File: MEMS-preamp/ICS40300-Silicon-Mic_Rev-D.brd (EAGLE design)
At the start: 14 x 15.7 mm, 8 parts, among them U1 ICS-40300, U2 MIC5225-3.3

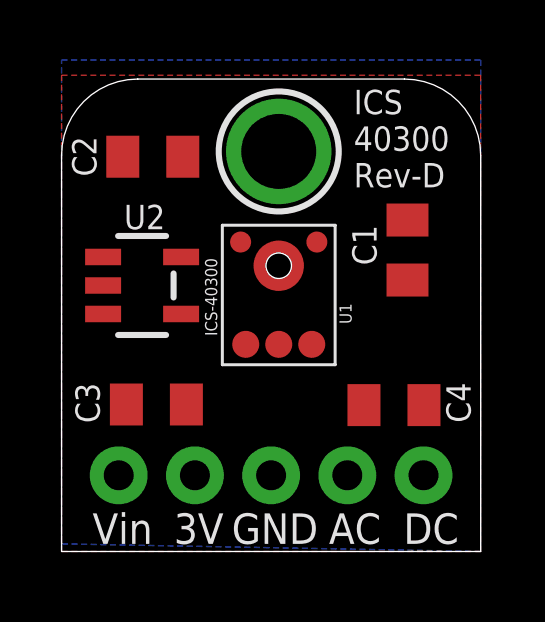
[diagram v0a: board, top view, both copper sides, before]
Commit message: test OPA analog mixers versions C-F
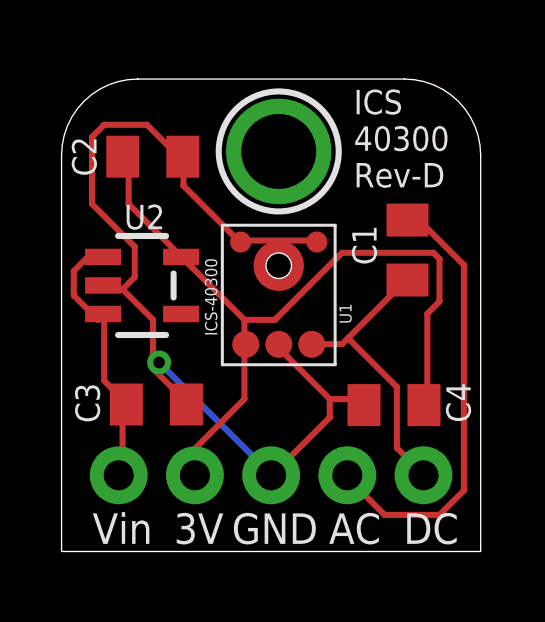
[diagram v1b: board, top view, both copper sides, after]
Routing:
- net GND: track 0.00 -> 33.7 mm, vias 0 -> 1
- net VDD: track 0.00 -> 25.6 mm
- net N$2: track 0.00 -> 14.8 mm
- net N$1: track 0.00 -> 9.68 mm
- net VIN: track 0.00 -> 9.22 mm
- removed copper zone on layer 1, net GND
- removed copper zone on layer 16, net GND
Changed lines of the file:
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@@
 <contactref element="C1" pad="1"/>
 <contactref element="JP1" pad="5"/>
-<wire x1="8.339" y1="6.905" x2="11.531" y2="9.048" width="0" layer="19" extent="1-1"/>
-<wire x1="12.065" y1="2.54" x2="11.531" y2="9.048" width="0" layer="19" extent="1-1"/>
+<wire x1="9.3472" y1="6.9088" x2="8.5344" y2="6.9088" width="0.2032" layer="1"/>
+<wire x1="11.3792" y1="8.9408" x2="9.5504" y2="7.112" width="0.2032" layer="1"/>
+<wire x1="9.5504" y1="7.112" x2="9.3472" y2="6.9088" width="0.2032" layer="1"/>
+<wire x1="8.5344" y1="6.9088" x2="8.339" y2="6.905" width="0.2032" layer="1"/>
+<wire x1="11.3792" y1="8.9408" x2="11.531" y2="9.048" width="0.2032" layer="1"/>
+<wire x1="11.176" y1="5.4864" x2="9.5504" y2="7.112" width="0.2032" layer="1"/>
+<wire x1="11.176" y1="3.4544" x2="11.176" y2="5.4864" width="0.2032" layer="1"/>
+<wire x1="11.9888" y1="2.6416" x2="11.176" y2="3.4544" width="0.2032" layer="1"/>
+<wire x1="11.9888" y1="2.6416" x2="12.065" y2="2.54" width="0.2032" layer="1"/>
 </signal>
 <signal name="GND">
 <contactref element="U2" pad="2"/>
 <contactref element="JP1" pad="3"/>
-<polygon width="0.254" layer="1" isolate="0.254">
-<vertex x="0" y="0"/>
-<vertex x="0" y="15.875"/>
-<vertex x="13.97" y="15.875"/>
-<vertex x="13.97" y="0"/>
-</polygon>
-<polygon width="0.254" layer="16" isolate="0.254">
-<vertex x="0" y="0.254"/>
-<vertex x="0" y="16.383"/>
-<vertex x="13.97" y="16.383"/>
-<vertex x="13.97" y="0"/>
-</polygon>
 <contactref element="U1" pad="GND3"/>
 <contactref element="U1" pad="GND"/>
@@
 <contactref element="C3" pad="2"/>
 <contactref element="C4" pad="2"/>
-<wire x1="4.16" y1="4.9" x2="10.08" y2="4.88" width="0" layer="19" extent="1-1"/>
-<wire x1="4.04" y1="13.16" x2="4.16" y2="4.9" width="0" layer="19" extent="1-1"/>
-<wire x1="6.985" y1="2.54" x2="4.04" y2="13.16" width="0" layer="19" extent="1-1"/>
-<wire x1="7.239" y1="6.905" x2="6.985" y2="2.54" width="0" layer="19" extent="1-1"/>
-<wire x1="7.239" y1="9.525" x2="7.239" y2="6.905" width="0" layer="19" extent="1-1"/>
-<wire x1="8.509" y1="10.315" x2="7.239" y2="9.525" width="0" layer="19" extent="1-1"/>
-<wire x1="5.969" y1="10.315" x2="7.239" y2="9.525" width="0" layer="19" extent="1-1"/>
-<wire x1="1.3839" y1="8.867" x2="5.969" y2="10.315" width="0" layer="19" extent="1-1"/>
+<wire x1="8.9408" y1="5.08" x2="7.3152" y2="6.7056" width="0.2032" layer="1"/>
+<wire x1="9.9568" y1="5.08" x2="8.9408" y2="5.08" width="0.2032" layer="1"/>
+<wire x1="7.3152" y1="6.7056" x2="7.239" y2="6.905" width="0.2032" layer="1"/>
+<wire x1="9.9568" y1="5.08" x2="10.08" y2="4.88" width="0.2032" layer="1"/>
+<wire x1="8.9408" y1="4.4704" x2="8.9408" y2="5.08" width="0.2032" layer="1"/>
+<wire x1="7.112" y1="2.6416" x2="8.9408" y2="4.4704" width="0.2032" layer="1"/>
+<wire x1="7.112" y1="2.6416" x2="6.985" y2="2.54" width="0.2032" layer="1"/>
+<wire x1="8.3312" y1="10.3632" x2="6.096" y2="10.3632" width="0.2032" layer="1"/>
+<wire x1="6.096" y1="10.3632" x2="5.969" y2="10.315" width="0.2032" layer="1"/>
+<wire x1="8.3312" y1="10.3632" x2="8.509" y2="10.315" width="0.2032" layer="1"/>
+<wire x1="4.064" y1="12.192" x2="4.064" y2="13.0048" width="0.2032" layer="1"/>
+<wire x1="5.8928" y1="10.3632" x2="4.064" y2="12.192" width="0.2032" layer="1"/>
+<wire x1="4.064" y1="13.0048" x2="4.04" y2="13.16" width="0.2032" layer="1"/>
+<wire x1="5.8928" y1="10.3632" x2="5.969" y2="10.315" width="0.2032" layer="1"/>
+<wire x1="2.032" y1="8.7376" x2="1.4224" y2="8.7376" width="0.2032" layer="1"/>
+<wire x1="3.048" y1="7.7216" x2="2.032" y2="8.7376" width="0.2032" layer="1"/>
+<wire x1="3.048" y1="6.096" x2="3.048" y2="6.2992" width="0.2032" layer="1"/>
+<wire x1="3.048" y1="6.2992" x2="3.048" y2="7.7216" width="0.2032" layer="1"/>
+<wire x1="4.064" y1="5.08" x2="3.048" y2="6.096" width="0.2032" layer="1"/>
+<wire x1="1.4224" y1="8.7376" x2="1.3839" y2="8.867" width="0.2032" layer="1"/>
+<wire x1="4.064" y1="5.08" x2="4.16" y2="4.9" width="0.2032" layer="1"/>
+<wire x1="2.8448" y1="14.224" x2="3.8608" y2="13.208" width="0.2032" layer="1"/>
+<wire x1="1.4224" y1="14.224" x2="2.8448" y2="14.224" width="0.2032" layer="1"/>
+<wire x1="1.016" y1="13.8176" x2="1.4224" y2="14.224" width="0.2032" layer="1"/>
+<wire x1="1.016" y1="11.5824" x2="1.016" y2="13.8176" width="0.2032" layer="1"/>
+<wire x1="2.4384" y1="10.16" x2="1.016" y2="11.5824" width="0.2032" layer="1"/>
+<wire x1="2.4384" y1="9.144" x2="2.4384" y2="10.16" width="0.2032" layer="1"/>
+<wire x1="2.032" y1="8.7376" x2="2.4384" y2="9.144" width="0.2032" layer="1"/>
+<wire x1="3.8608" y1="13.208" x2="4.04" y2="13.16" width="0.2032" layer="1"/>
+<wire x1="3.2512" y1="6.2992" x2="6.9088" y2="2.6416" width="0.2032" layer="16"/>
+<wire x1="3.048" y1="6.2992" x2="3.2512" y2="6.2992" width="0.2032" layer="1"/>
+<wire x1="6.9088" y1="2.6416" x2="6.985" y2="2.54" width="0.2032" layer="16"/>
+<via x="3.2512" y="6.2992" extent="1-16" drill="0.3937"/>
+<wire x1="8.3312" y1="10.3632" x2="7.239" y2="9.525" width="0" layer="19" extent="1-1"/>
 </signal>
 <signal name="VDD">
@@
 <contactref element="C2" pad="1"/>
 <contactref element="C4" pad="1"/>
-<wire x1="2.04" y1="13.16" x2="12.08" y2="4.88" width="0" layer="19" extent="1-1"/>
-<wire x1="4.445" y1="2.54" x2="2.04" y2="13.16" width="0" layer="19" extent="1-1"/>
-<wire x1="6.139" y1="6.905" x2="4.445" y2="2.54" width="0" layer="19" extent="1-1"/>
-<wire x1="3.9841" y1="9.817" x2="6.139" y2="6.905" width="0" layer="19" extent="1-1"/>
+<wire x1="6.096" y1="7.7216" x2="6.096" y2="6.9088" width="0.2032" layer="1"/>
+<wire x1="4.064" y1="9.7536" x2="6.096" y2="7.7216" width="0.2032" layer="1"/>
+<wire x1="6.096" y1="6.9088" x2="6.139" y2="6.905" width="0.2032" layer="1"/>
+<wire x1="4.064" y1="9.7536" x2="3.9841" y2="9.817" width="0.2032" layer="1"/>
+<wire x1="12.192" y1="7.9248" x2="12.192" y2="5.08" width="0.2032" layer="1"/>
+<wire x1="12.5984" y1="8.3312" x2="12.192" y2="7.9248" width="0.2032" layer="1"/>
+<wire x1="12.5984" y1="9.7536" x2="12.5984" y2="8.3312" width="0.2032" layer="1"/>
+<wire x1="12.3952" y1="9.9568" x2="12.5984" y2="9.7536" width="0.2032" layer="1"/>
+<wire x1="9.3472" y1="9.9568" x2="12.3952" y2="9.9568" width="0.2032" layer="1"/>
+<wire x1="7.112" y1="7.7216" x2="9.3472" y2="9.9568" width="0.2032" layer="1"/>
+<wire x1="6.096" y1="7.7216" x2="7.112" y2="7.7216" width="0.2032" layer="1"/>
+<wire x1="12.192" y1="5.08" x2="12.08" y2="4.88" width="0.2032" layer="1"/>
+<wire x1="2.2352" y1="11.5824" x2="2.2352" y2="13.0048" width="0.2032" layer="1"/>
+<wire x1="3.8608" y1="9.9568" x2="2.2352" y2="11.5824" width="0.2032" layer="1"/>
+<wire x1="2.2352" y1="13.0048" x2="2.04" y2="13.16" width="0.2032" layer="1"/>
+<wire x1="3.8608" y1="9.9568" x2="3.9841" y2="9.817" width="0.2032" layer="1"/>
+<wire x1="4.4704" y1="3.4544" x2="4.4704" y2="2.6416" width="0.2032" layer="1"/>
+<wire x1="6.096" y1="5.08" x2="4.4704" y2="3.4544" width="0.2032" layer="1"/>
+<wire x1="6.096" y1="6.7056" x2="6.096" y2="5.08" width="0.2032" layer="1"/>
+<wire x1="4.4704" y1="2.6416" x2="4.445" y2="2.54" width="0.2032" layer="1"/>
+<wire x1="6.096" y1="6.7056" x2="6.139" y2="6.905" width="0.2032" layer="1"/>
 </signal>
 <signal name="N$2">
 <contactref element="JP1" pad="4"/>
 <contactref element="C1" pad="2"/>
-<wire x1="9.525" y1="2.54" x2="11.531" y2="11.048" width="0" layer="19" extent="1-1"/>
+<wire x1="11.9888" y1="10.9728" x2="11.5824" y2="10.9728" width="0.2032" layer="1"/>
+<wire x1="13.4112" y1="9.5504" x2="11.9888" y2="10.9728" width="0.2032" layer="1"/>
+<wire x1="13.4112" y1="2.032" x2="13.4112" y2="9.5504" width="0.2032" layer="1"/>
+<wire x1="12.5984" y1="1.2192" x2="13.4112" y2="2.032" width="0.2032" layer="1"/>
+<wire x1="10.7696" y1="1.2192" x2="12.5984" y2="1.2192" width="0.2032" layer="1"/>
+<wire x1="9.5504" y1="2.4384" x2="10.7696" y2="1.2192" width="0.2032" layer="1"/>
+<wire x1="11.5824" y1="10.9728" x2="11.531" y2="11.048" width="0.2032" layer="1"/>
+<wire x1="9.5504" y1="2.4384" x2="9.525" y2="2.54" width="0.2032" layer="1"/>
 </signal>
 <signal name="VIN">
@@
 <contactref element="JP1" pad="1"/>
 <contactref element="C3" pad="1"/>
-<wire x1="1.905" y1="2.54" x2="2.16" y2="4.9" width="0" layer="19" extent="1-1"/>
-<wire x1="1.3839" y1="7.917" x2="1.905" y2="2.54" width="0" layer="19" extent="1-1"/>
-<wire x1="1.3839" y1="9.817" x2="1.3839" y2="7.917" width="0" layer="19" extent="1-1"/>
+<wire x1="1.4224" y1="5.6896" x2="1.4224" y2="7.7216" width="0.2032" layer="1"/>
+<wire x1="2.032" y1="5.08" x2="1.4224" y2="5.6896" width="0.2032" layer="1"/>
+<wire x1="1.4224" y1="7.7216" x2="1.3839" y2="7.917" width="0.2032" layer="1"/>
+<wire x1="2.032" y1="5.08" x2="2.16" y2="4.9" width="0.2032" layer="1"/>
+<wire x1="0.8128" y1="9.7536" x2="1.2192" y2="9.7536" width="0.2032" layer="1"/>
+<wire x1="0.4064" y1="9.3472" x2="0.8128" y2="9.7536" width="0.2032" layer="1"/>
+<wire x1="0.4064" y1="8.5344" x2="0.4064" y2="9.3472" width="0.2032" layer="1"/>
+<wire x1="1.2192" y1="7.7216" x2="0.4064" y2="8.5344" width="0.2032" layer="1"/>
+<wire x1="1.2192" y1="9.7536" x2="1.3839" y2="9.817" width="0.2032" layer="1"/>
+<wire x1="1.2192" y1="7.7216" x2="1.3839" y2="7.917" width="0.2032" layer="1"/>
+<wire x1="2.032" y1="2.6416" x2="2.032" y2="4.8768" width="0.2032" layer="1"/>
+<wire x1="2.032" y1="4.8768" x2="2.16" y2="4.9" width="0.2032" layer="1"/>
+<wire x1="2.032" y1="2.6416" x2="1.905" y2="2.54" width="0.2032" layer="1"/>
 </signal>
 </signals>
